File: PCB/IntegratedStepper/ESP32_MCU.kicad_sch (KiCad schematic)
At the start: 25 parts, among them Q1 SS8050-G, Q2 SS8050-G, U1 ESP32-WROOM-32E, U3 CP2102N-Axx-xQFN28

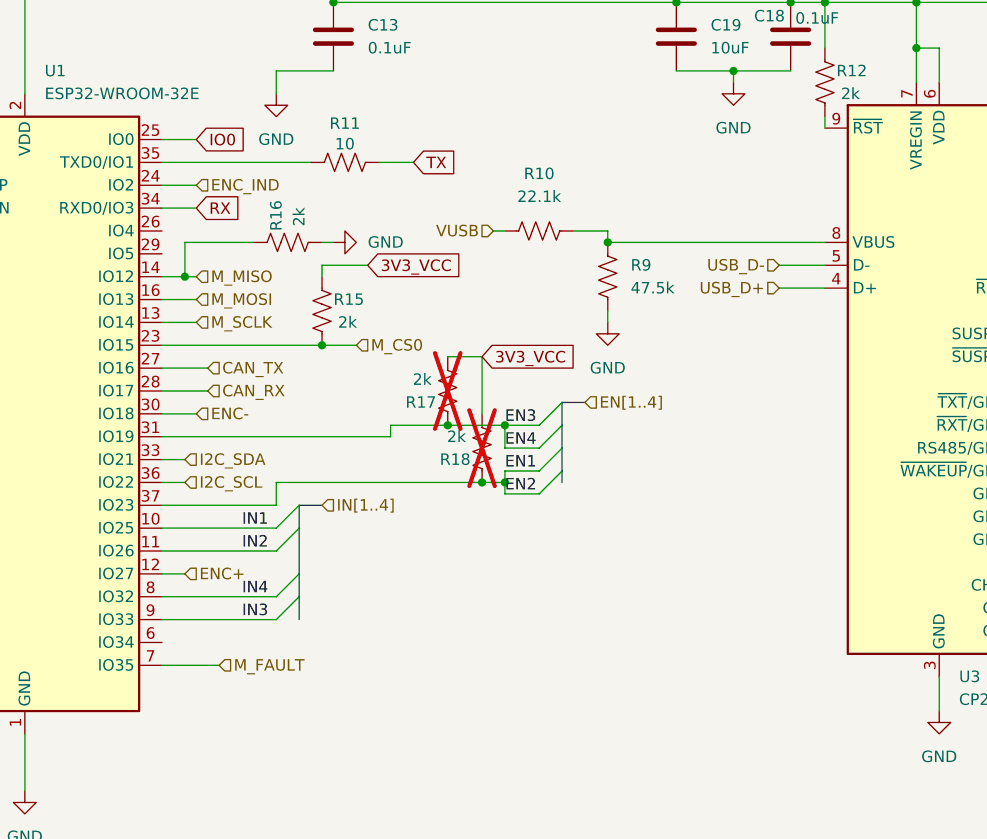
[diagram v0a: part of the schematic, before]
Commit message: Update PCB with DRV8243 for 12A capacity
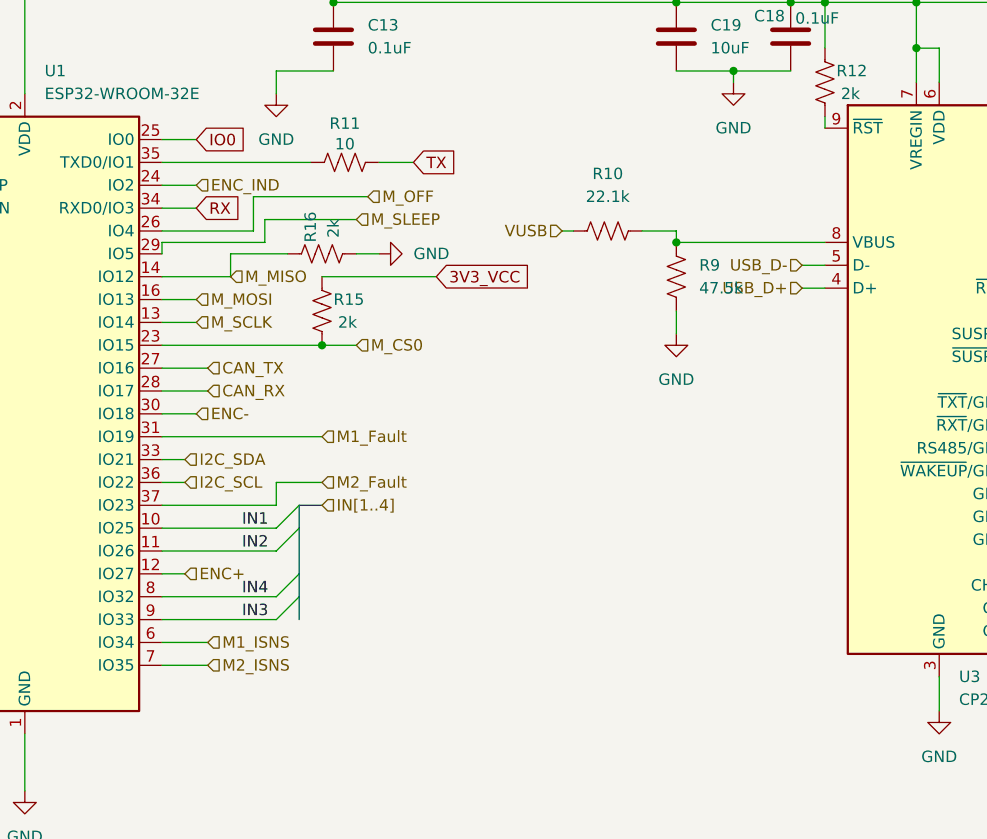
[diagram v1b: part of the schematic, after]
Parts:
- removed R17, R18: 2k, Resistor_SMD:R_0603_1608Metric, symbol Device:R_US
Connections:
- net M_OFF: now reaches U1.26 (IO4)
- net M_SLEEP: now reaches U1.29 (IO5)
- net M1_ISNS: now reaches U1.6 (IO34)
- net EN1 renamed M2_Fault
- net EN3 renamed M1_Fault
- net M_FAULT renamed M2_ISNS
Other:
- moved on the sheet: R10, R16, R9

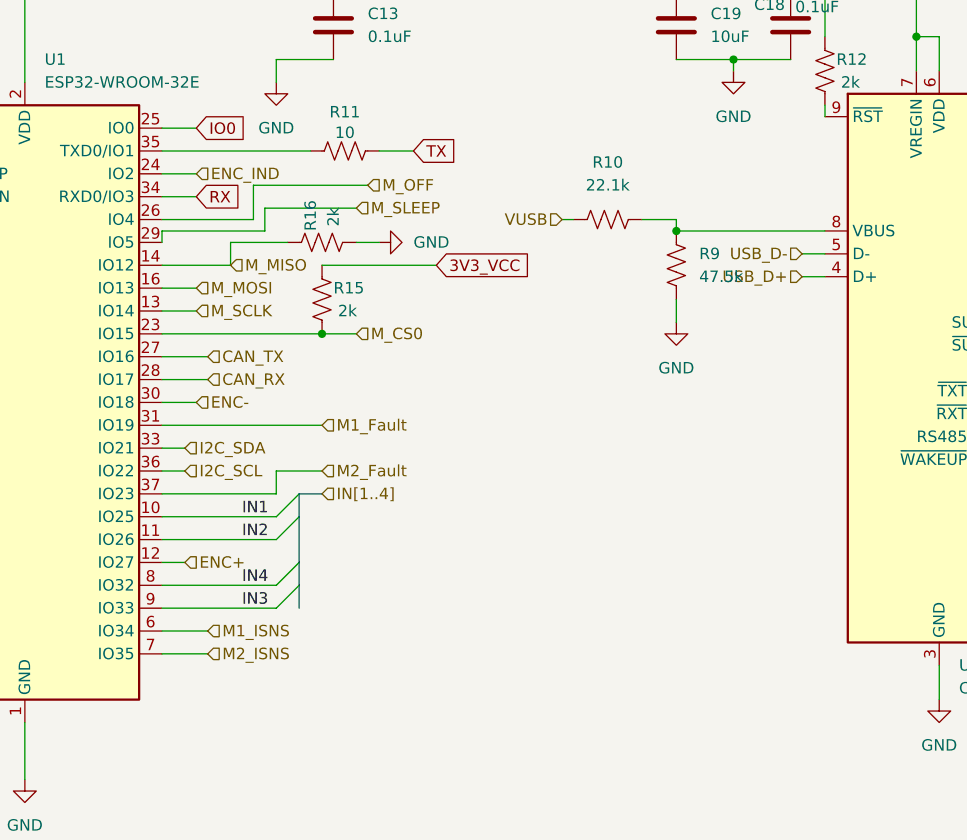
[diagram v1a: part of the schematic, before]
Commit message: update layout with pinout changes
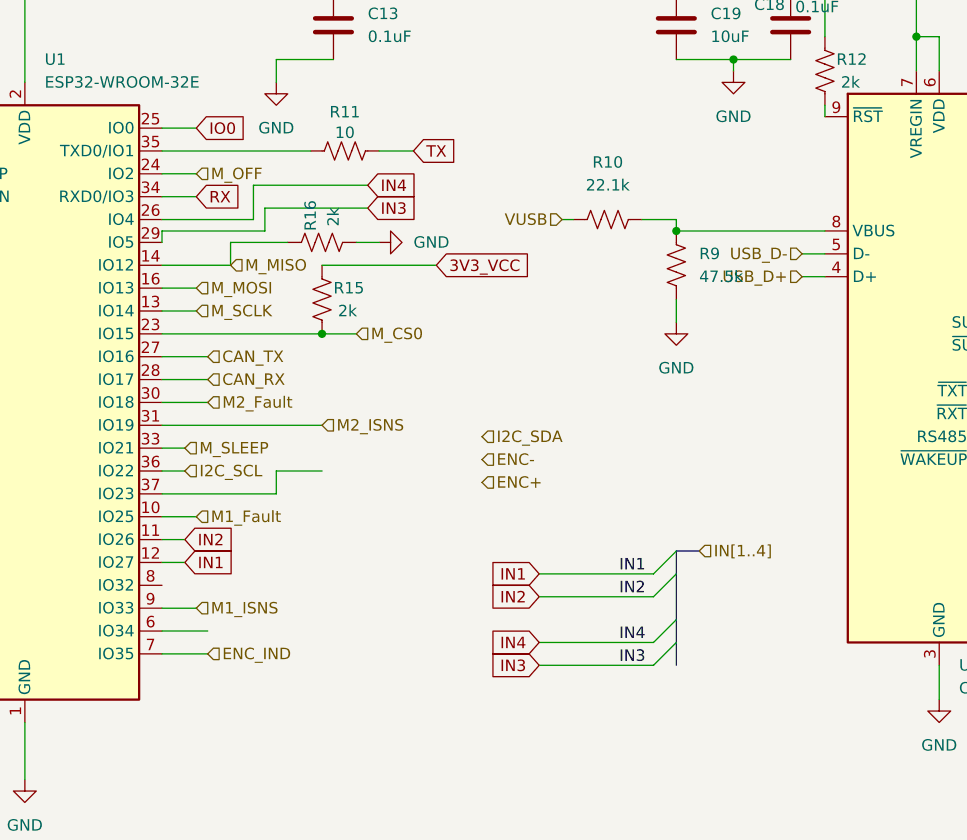
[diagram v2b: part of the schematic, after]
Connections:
- net ENC+: no longer U1.12 (IO27)
- net ENC-: no longer U1.30 (IO18)
- net ENC_IND: now also U1.7 (IO35); no longer U1.24 (IO2)
- net I2C_SDA: no longer U1.33 (IO21)
- net IN1: now also U1.12 (IO27); no longer U1.10 (IO25)
- net IN3: now also U1.29 (IO5); no longer U1.9 (IO33)
- net IN4: now also U1.26 (IO4); no longer U1.8 (IO32)
- net M1_Fault: now also U1.10 (IO25); no longer U1.31 (IO19)
- net M1_ISNS: now also U1.9 (IO33); no longer U1.6 (IO34)
- net M2_Fault: now also U1.30 (IO18); no longer U1.37 (IO23)
- net M2_ISNS: now also U1.31 (IO19); no longer U1.7 (IO35)
- net M_OFF: now also U1.24 (IO2); no longer U1.26 (IO4)
- net M_SLEEP: now also U1.33 (IO21); no longer U1.29 (IO5)

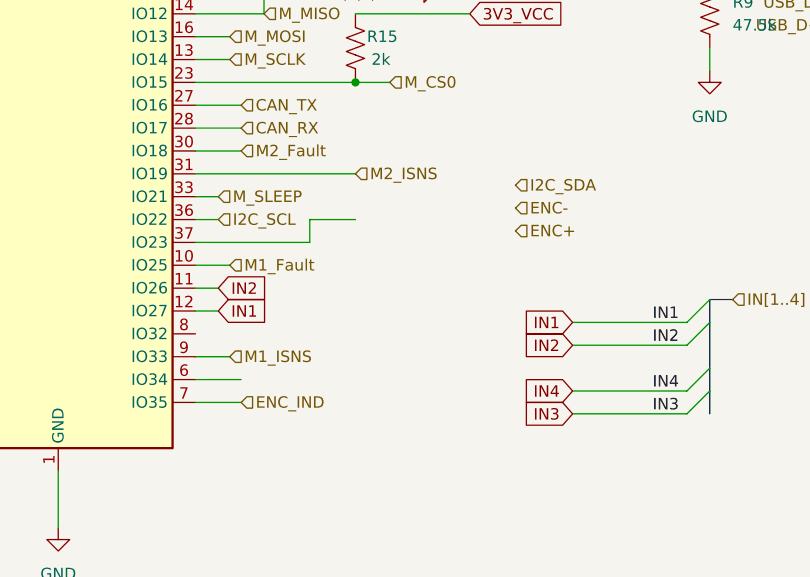
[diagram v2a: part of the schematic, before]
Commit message: finalize layout w/ thermals
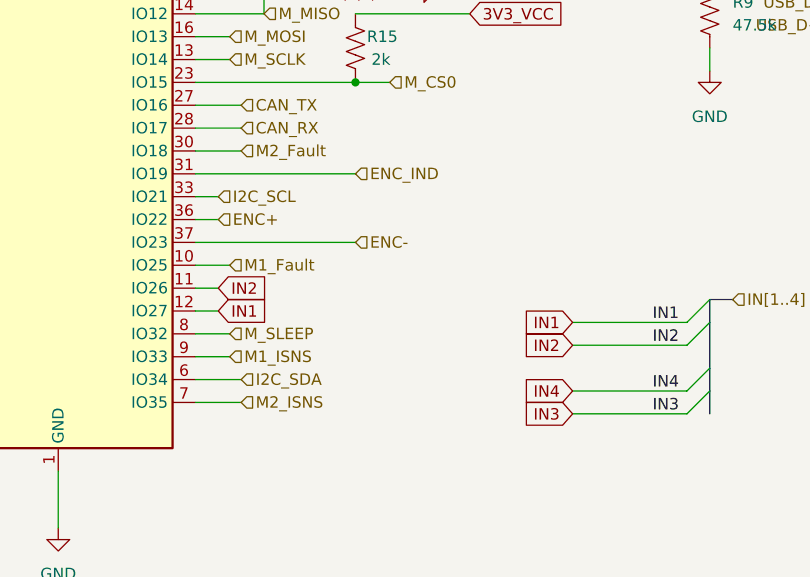
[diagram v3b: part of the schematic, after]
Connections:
- net ENC+: now also U1.36 (IO22)
- net ENC-: now also U1.37 (IO23)
- net ENC_IND: now also U1.31 (IO19); no longer U1.7 (IO35)
- net I2C_SCL: now also U1.33 (IO21); no longer U1.36 (IO22)
- net I2C_SDA: now also U1.6 (IO34)
- net M2_ISNS: now also U1.7 (IO35); no longer U1.31 (IO19)
- net M_SLEEP: now also U1.8 (IO32); no longer U1.33 (IO21)
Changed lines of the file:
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@@
 	(wire
 		(pts
-			(xy 132.08 95.25) (xy 144.78 95.25)
+			(xy 132.08 95.25) (xy 149.86 95.25)
 		)
 		(stroke
@@
 	(wire
 		(pts
-			(xy 144.78 95.25) (xy 144.78 92.71)
-		)
-		(stroke
-			(width 0)
-			(type default)
-		)
-	)
-	(wire
-		(pts
 			(xy 142.24 64.77) (xy 142.24 60.96)
 		)
@@
 	(wire
 		(pts
+			(xy 135.89 105.41) (xy 132.08 105.41)
+		)
+		(stroke
+			(width 0)
+			(type default)
+		)
+	)
+	(wire
+		(pts
 			(xy 55.88 147.32) (xy 67.31 147.32)
 		)
@@
 		(pts
 			(xy 132.08 72.39) (xy 135.89 72.39)
-		)
-		(stroke
-			(width 0)
-			(type default)
-		)
-	)
-	(wire
-		(pts
-			(xy 144.78 92.71) (xy 149.86 92.71)
 		)
 		(stroke
@@
 		)
 	)
+	(hierarchical_label "CAN_RX"
+		(shape input)
+		(at 137.16 82.55 0)
+		(fields_autoplaced yes)
+		(effects
+			(font
+				(size 1.27 1.27)
+			)
+			(justify left)
+		)
+	)
+	(hierarchical_label "M_OFF"
+		(shape input)
+		(at 135.89 59.69 0)
+		(fields_autoplaced yes)
+		(effects
+			(font
+				(size 1.27 1.27)
+			)
+			(justify left)
+		)
+	)
+	(hierarchical_label "M_CS0"
+		(shape input)
+		(at 153.67 77.47 0)
+		(fields_autoplaced yes)
+		(effects
+			(font
+				(size 1.27 1.27)
+			)
+			(justify left)
+		)
+	)
+	(hierarchical_label "USB_D-"
+		(shape input)
+		(at 203.2 68.58 180)
+		(fields_autoplaced yes)
+		(effects
+			(font
+				(size 1.27 1.27)
+			)
+			(justify right)
+		)
+	)
+	(hierarchical_label "M_SCLK"
+		(shape input)
+		(at 135.89 74.93 0)
+		(fields_autoplaced yes)
+		(effects
+			(font
+				(size 1.27 1.27)
+			)
+			(justify left)
+		)
+	)
+	(hierarchical_label "M1_ISNS"
+		(shape input)
+		(at 135.89 107.95 0)
+		(fields_autoplaced yes)
+		(effects
+			(font
+				(size 1.27 1.27)
+			)
+			(justify left)
+		)
+	)
+	(hierarchical_label "M2_ISNS"
+		(shape input)
+		(at 137.16 113.03 0)
+		(fields_autoplaced yes)
+		(effects
+			(font
+				(size 1.27 1.27)
+			)
+			(justify left)
+		)
+	)
+	(hierarchical_label "I2C_SDA"
+		(shape input)
+		(at 137.16 110.49 0)
+		(fields_autoplaced yes)
+		(effects
+			(font
+				(size 1.27 1.27)
+			)
+			(justify left)
+		)
+	)
+	(hierarchical_label "M1_Fault"
+		(shape input)
+		(at 135.89 97.79 0)
+		(fields_autoplaced yes)
+		(effects
+			(font
+				(size 1.27 1.27)
+			)
+			(justify left)
+		)
+	)
+	(hierarchical_label "ENC_IND"
+		(shape input)
+		(at 149.86 87.63 0)
+		(fields_autoplaced yes)
+		(effects
+			(font
+				(size 1.27 1.27)
+			)
+			(justify left)
+		)
+	)
+	(hierarchical_label "USB_D+"
+		(shape input)
+		(at 203.2 71.12 180)
+		(fields_autoplaced yes)
+		(effects
+			(font
+				(size 1.27 1.27)
+			)
+			(justify right)
+		)
+	)
+	(hierarchical_label "M_SLEEP"
+		(shape input)
+		(at 135.89 105.41 0)
+		(fields_autoplaced yes)
+		(effects
+			(font
+				(size 1.27 1.27)
+			)
+			(justify left)
+		)
+	)
+	(hierarchical_label "IN[1..4]"
+		(shape input)
+		(at 191.77 101.6 0)
+		(fields_autoplaced yes)
+		(effects
+			(font
+				(size 1.27 1.27)
+			)
+			(justify left)
+		)
+	)
+	(hierarchical_label "3V3_VCC"
+		(shape input)
+		(at 229.87 39.37 0)
+		(fields_autoplaced yes)
+		(effects
+			(font
+				(size 1.27 1.27)
+			)
+			(justify left)
+		)
+	)
+	(hierarchical_label "ENC-"
+		(shape input)
+		(at 149.86 95.25 0)
+		(fields_autoplaced yes)
+		(effects
+			(font
+				(size 1.27 1.27)
+			)
+			(justify left)
+		)
+	)
+	(hierarchical_label "VUSB"
+		(shape input)
+		(at 176.53 64.77 180)
+		(fields_autoplaced yes)
+		(effects
+			(font
+				(size 1.27 1.27)
+			)
+			(justify right)
+		)
+	)
+	(hierarchical_label "I2C_SCL"
+		(shape input)
+		(at 134.62 90.17 0)
+		(fields_autoplaced yes)
+		(effects
+			(font
+				(size 1.27 1.27)
+			)
+			(justify left)
+		)
+	)
 	(hierarchical_label "ENC+"
 		(shape input)
-		(at 167.64 93.98 0)
-		(fields_autoplaced yes)
-		(effects
-			(font
-				(size 1.27 1.27)
-			)
-			(justify left)
-		)
-	)
-	(hierarchical_label "CAN_RX"
-		(shape input)
-		(at 137.16 82.55 0)
-		(fields_autoplaced yes)
-		(effects
-			(font
-				(size 1.27 1.27)
-			)
-			(justify left)
-		)
-	)
-	(hierarchical_label "M_OFF"
-		(shape input)
-		(at 135.89 59.69 0)
-		(fields_autoplaced yes)
-		(effects
-			(font
-				(size 1.27 1.27)
-			)
-			(justify left)
-		)
-	)
-	(hierarchical_label "M_CS0"
-		(shape input)
-		(at 153.67 77.47 0)
-		(fields_autoplaced yes)
-		(effects
-			(font
-				(size 1.27 1.27)
-			)
-			(justify left)
-		)
-	)
-	(hierarchical_label "USB_D-"
-		(shape input)
-		(at 203.2 68.58 180)
-		(fields_autoplaced yes)
-		(effects
-			(font
-				(size 1.27 1.27)
-			)
-			(justify right)
-		)
-	)
-	(hierarchical_label "M2_ISNS"
-		(shape input)
-		(at 149.86 87.63 0)
-		(fields_autoplaced yes)
-		(effects
-			(font
-				(size 1.27 1.27)
-			)
-			(justify left)
-		)
-	)
-	(hierarchical_label "I2C_SCL"
-		(shape input)
 		(at 134.62 92.71 0)
 		(fields_autoplaced yes)
 		(effects
-			(font
-				(size 1.27 1.27)
-			)
-			(justify left)
-		)
-	)
-	(hierarchical_label "M_SCLK"
-		(shape input)
-		(at 135.89 74.93 0)
-		(fields_autoplaced yes)
-		(effects
-			(font
-				(size 1.27 1.27)
-			)
-			(justify left)
-		)
-	)
-	(hierarchical_label "M1_ISNS"
-		(shape input)
-		(at 135.89 107.95 0)
-		(fields_autoplaced yes)
-		(effects
-			(font
-				(size 1.27 1.27)
-			)
-			(justify left)
-		)
-	)
-	(hierarchical_label "I2C_SDA"
-		(shape input)
-		(at 167.64 88.9 0)
-		(fields_autoplaced yes)
-		(effects
-			(font
-				(size 1.27 1.27)
-			)
-			(justify left)
-		)
-	)
-	(hierarchical_label "ENC-"
-		(shape input)
-		(at 167.64 91.44 0)
-		(fields_autoplaced yes)
-		(effects
-			(font
-				(size 1.27 1.27)
-			)
-			(justify left)
-		)
-	)
-	(hierarchical_label "M1_Fault"
-		(shape input)
-		(at 135.89 97.79 0)
-		(fields_autoplaced yes)
-		(effects
-			(font
-				(size 1.27 1.27)
-			)
-			(justify left)
-		)
-	)
-	(hierarchical_label "USB_D+"
-		(shape input)
-		(at 203.2 71.12 180)
-		(fields_autoplaced yes)
-		(effects
-			(font
-				(size 1.27 1.27)
-			)
-			(justify right)
-		)
-	)
-	(hierarchical_label "IN[1..4]"
-		(shape input)
-		(at 191.77 101.6 0)
-		(fields_autoplaced yes)
-		(effects
-			(font
-				(size 1.27 1.27)
-			)
-			(justify left)
-		)
-	)
-	(hierarchical_label "3V3_VCC"
-		(shape input)
-		(at 229.87 39.37 0)
-		(fields_autoplaced yes)
-		(effects
-			(font
-				(size 1.27 1.27)
-			)
-			(justify left)
-		)
-	)
-	(hierarchical_label "VUSB"
-		(shape input)
-		(at 176.53 64.77 180)
-		(fields_autoplaced yes)
-		(effects
-			(font
-				(size 1.27 1.27)
-			)
-			(justify right)
-		)
-	)
-	(hierarchical_label "ENC_IND"
-		(shape input)
-		(at 137.16 113.03 0)
-		(fields_autoplaced yes)
-		(effects
-			(font
-				(size 1.27 1.27)
-			)
-			(justify left)
-		)
-	)
-	(hierarchical_label "M_SLEEP"
-		(shape input)
-		(at 134.62 90.17 0)
-		(fields_autoplaced yes)
-		(effects

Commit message: Update final layout, replace CAN w/ JST
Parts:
- C13, C14, C18, C20, C21: LCSC C2929200 -> C5186689; LCSC Part C2929200 -> C5186689; LCSC Part Number C2929200 -> C5186689
- R13, R14: value 10k -> 8.2k; LCSC C469659 -> C25981; LCSC Part C469659 -> C25981; LCSC Part Number C469659 -> C25981
- R15, R16: value 2k -> 8.2k; LCSC C217936 -> C25981; LCSC Part C217936 -> C25981; LCSC Part Number C217936 -> C25981
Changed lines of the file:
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@@
 			)
 		)
-		(property "Value" "2k"
+		(property "Value" "8.2k"
 			(at 151.638 74.93 0)
 			(effects
@@
 			)
 		)
-		(property "LCSC" "C217936"
+		(property "LCSC" "C25981"
 			(at 149.86 73.66 0)
 			(effects
@@
 			)
 		)
-		(property "LCSC Part" "C217936"
+		(property "LCSC Part" "C25981"
 			(at 149.86 73.66 0)
 			(effects
@@
 			)
 		)
-		(property "LCSC Part Number" "C217936"
+		(property "LCSC Part Number" "C25981"
 			(at 149.86 73.66 0)
 			(effects
@@
 			)
 		)
-		(property "LCSC" "C2929200"
+		(property "LCSC" "C5186689"
 			(at 151.13 43.18 0)
 			(effects
@@
 			)
 		)
-		(property "LCSC Part Number" "C2929200"
+		(property "LCSC Part Number" "C5186689"
 			(at 151.13 43.18 0)
 			(effects
@@
 			)
 		)
-		(property "LCSC Part" "C2929200"
+		(property "LCSC Part" "C5186689"
 			(at 151.13 43.18 0)
 			(effects
@@
 			)
 		)
-		(property "LCSC" "C2929200"
+		(property "LCSC" "C5186689"
 			(at 201.93 43.18 0)
 			(effects
@@
 			)
 		)
-		(property "LCSC Part Number" "C2929200"
+		(property "LCSC Part Number" "C5186689"
 			(at 201.93 43.18 0)
 			(effects
@@
 			)
 		)
-		(property "LCSC Part" "C2929200"
+		(property "LCSC Part" "C5186689"
 			(at 201.93 43.18 0)
 			(effects
@@
 			)
 		)
-		(property "Value" "10k"
+		(property "Value" "8.2k"
 			(at 52.07 143.51 90)
 			(effects
@@
 			)
 		)
-		(property "LCSC" "C469659"
+		(property "LCSC" "C25981"
 			(at 52.07 147.32 0)
 			(effects
@@
 			)
 		)
-		(property "LCSC Part" "C469659"
+		(property "LCSC Part" "C25981"
 			(at 52.07 147.32 0)
 			(effects
@@
 			)
 		)
-		(property "LCSC Part Number" "C469659"
+		(property "LCSC Part Number" "C25981"
 			(at 52.07 147.32 0)
 			(effects
@@
 			)
 		)
-		(property "LCSC" "C2929200"
+		(property "LCSC" "C5186689"
 			(at 87.63 58.42 0)
 			(effects
@@
 			)
 		)
-		(property "LCSC Part Number" "C2929200"
+		(property "LCSC Part Number" "C5186689"
 			(at 87.63 58.42 0)
 			(effects
@@
 			)
 		)
-		(property "LCSC Part" "C2929200"
+		(property "LCSC Part" "C5186689"
 			(at 87.63 58.42 0)
 			(effects
@@
 			)
 		)
-		(property "LCSC" "C2929200"
+		(property "LCSC" "C5186689"
 			(at 120.65 146.05 0)
 			(effects
@@
 			)
 		)
-		(property "LCSC Part Number" "C2929200"
+		(property "LCSC Part Number" "C5186689"
 			(at 120.65 146.05 0)
 			(effects
@@
 			)
 		)
-		(property "LCSC Part" "C2929200"
+		(property "LCSC Part" "C5186689"
 			(at 120.65 146.05 0)
 			(effects
@@
 			)
 		)
-		(property "Value" "10k"
+		(property "Value" "8.2k"
 			(at 57.15 167.64 90)
 			(effects
@@
 			)
 		)
-		(property "LCSC" "C469659"
+		(property "LCSC" "C25981"
 			(at 57.15 171.45 0)
 			(effects
@@
 			)
 		)
-		(property "LCSC Part" "C469659"
+		(property "LCSC Part" "C25981"
 			(at 57.15 171.45 0)
 			(effects
@@
 			)
 		)
-		(property "LCSC Part Number" "C469659"
+		(property "LCSC Part Number" "C25981"
 			(at 57.15 171.45 0)
 			(effects
@@
 			)
 		)
-		(property "Value" "2k"
+		(property "Value" "8.2k"
 			(at 151.13 65.532 0)
 			(effects
@@
 			)
 		)
-		(property "LCSC" "C217936"
+		(property "LCSC" "C25981"
 			(at 149.86 67.31 0)
 			(effects
@@
 			)
 		)
-		(property "LCSC Part" "C217936"
+		(property "LCSC Part" "C25981"
 			(at 149.86 67.31 0)
 			(effects
@@
 			)
 		)
-		(property "LCSC Part Number" "C217936"
+		(property "LCSC Part Number" "C25981"
 			(at 149.86 67.31 0)
 			(effects
@@
 			)
 		)
-		(property "LCSC" "C2929200"
+		(property "LCSC" "C5186689"
 			(at 121.92 172.72 0)
 			(effects
@@
 			)
 		)
-		(property "LCSC Part Number" "C2929200"
+		(property "LCSC Part Number" "C5186689"
 			(at 121.92 172.72 0)
 			(effects
@@
 			)
 		)
-		(property "LCSC Part" "C2929200"
+		(property "LCSC Part" "C5186689"
 			(at 121.92 172.72 0)
 			(effects

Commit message: update new tester board sch
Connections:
- net I2C_SCL renamed DRV1_CS
- net I2C_SDA renamed DRV2_CS
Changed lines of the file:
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@@
 		)
 	)
-	(hierarchical_label "I2C_SDA"
+	(hierarchical_label "DRV2_CS"
 		(shape input)
 		(at 137.16 110.49 0)
@@
 		)
 	)
-	(hierarchical_label "I2C_SCL"
+	(hierarchical_label "DRV1_CS"
 		(shape input)
 		(at 134.62 90.17 0)
